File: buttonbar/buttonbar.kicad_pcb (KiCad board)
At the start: 2 copper layers, 65.9 x 54.7 mm, 44 parts, among them J1 Conn_01x08_Male, J2 Conn_01x06_Male, SW1 SW_Push, SW2 SW_Push, SW3 SW_Push, SW4 SW_Push, SW5 SW_Push, SW6 SW_Push, U1 74HC14D

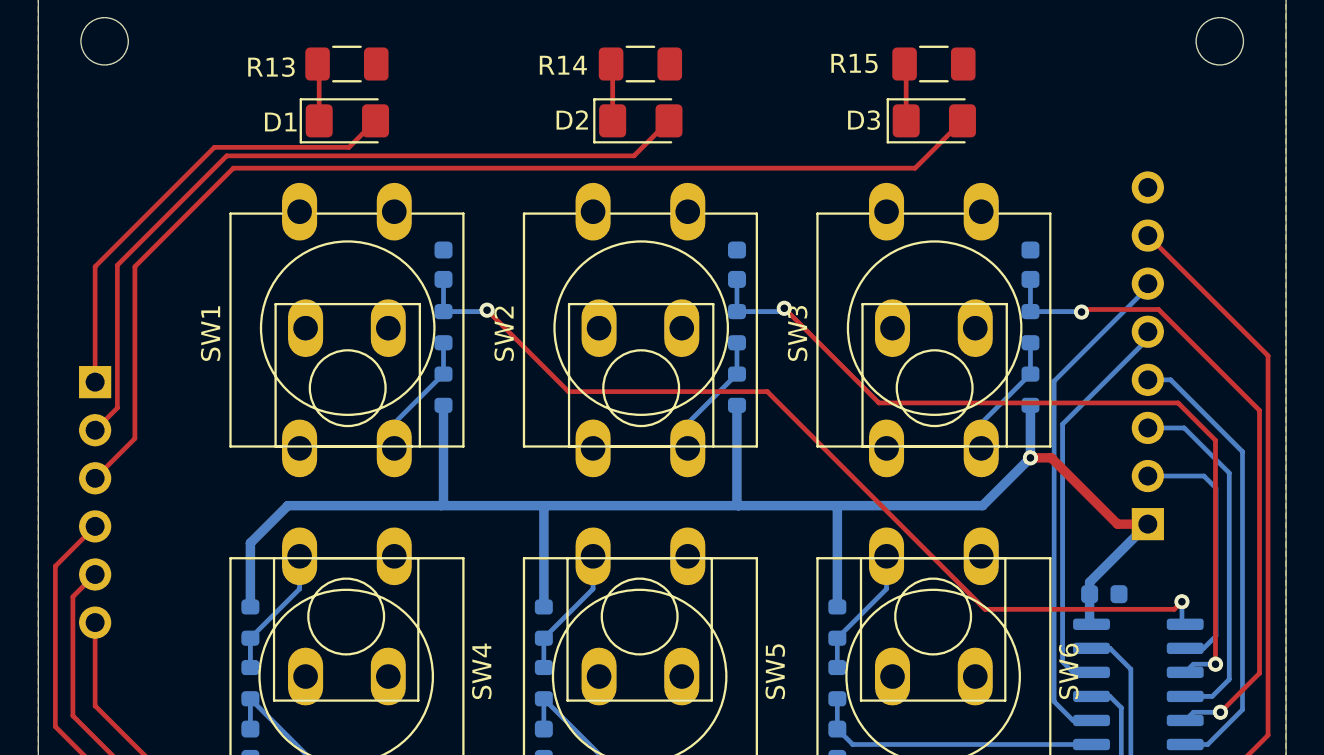
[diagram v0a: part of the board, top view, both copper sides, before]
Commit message: Rev 1.1: added labels (no functional change)
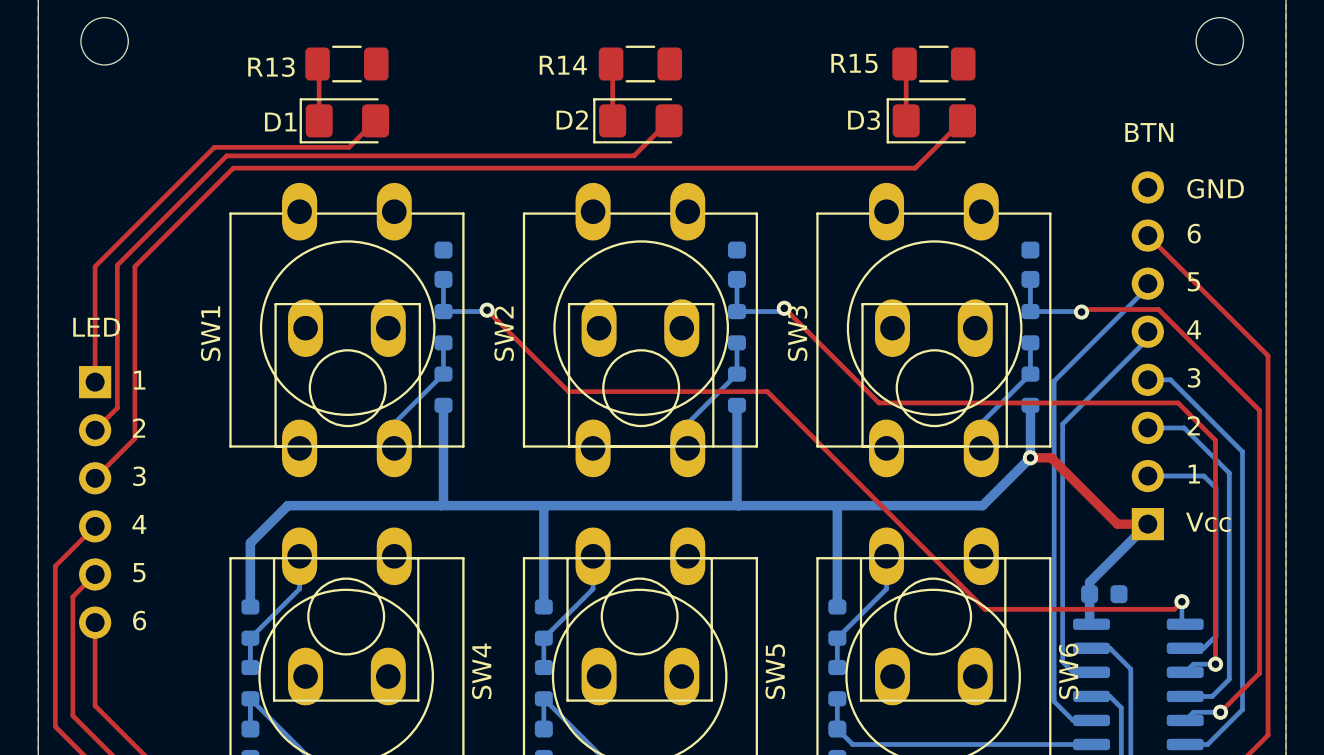
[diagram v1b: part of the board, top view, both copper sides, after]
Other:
- board text added: "2"
- board text added: "3"
- board text added: "4"
- board text added: "5"
- board text added: "6"
- board text added: "BTN"
- board text added: "GND"
- board text added: "LED"
- board text added: "Vcc"
- board text added: "https://github.com/bablokb/pcb-buttonbar Rev 1.1"
- board text removed: "https://github.com/bablokb/pcb-buttonbar Rev 1.0"

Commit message: migrated to Kicad 6
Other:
- net class Default removed
- net class Vcc removed

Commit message: Rev 2.1
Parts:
- added J3: Conn_01x04_Male, Connector_PinHeader_2.54mm:PinHeader_1x04_P2.54mm_Vertical, B.Cu at (149.7, 113.8)
- J1: value Conn_01x08_Male -> Conn_01x04_Male; footprint Connector_PinHeader_2.54mm:PinHeader_1x08_P2.54mm_Vertical -> Connector_PinHeader_2.54mm:PinHeader_1x04_P2.54mm_Vertical
- R13, R14, R15, R16, R17, R18: value 680 1206 -> 680 0603; footprint Resistor_SMD:R_1206_3216Metric_Pad1.30x1.75mm_HandSolder -> Resistor_SMD:R_0603_1608Metric; moved to B.Cu
- SW1, SW2, SW3, SW4, SW5, SW6: footprint user:SW_PUSH-6.12mm -> user:SW_PUSH_5.08mm
- moved H4 80.0 mm to (94.8, 117.0)
- moved J1 69.0 mm to (111.4, 113.8), turned to -90 degrees
- moved H3 67.8 mm to (173.8, 117.0)
- moved H2 61.1 mm to (173.8, 88.0)
- moved C3 57.8 mm to (130.4, 109.4), turned to 0 degrees
- moved R6 57.1 mm to (127.1, 109.4), turned to 180 degrees
- moved R5 56.6 mm to (123.9, 109.4), turned to 0 degrees
- moved C2 55.9 mm to (118.5, 109.4), turned to 0 degrees
- moved R4 54.9 mm to (115.2, 109.4), turned to 180 degrees
- moved C1 54.8 mm to (105.6, 109.6), turned to 0 degrees
- moved R3 54.3 mm to (111.9, 109.4), turned to 0 degrees
- moved R2 53.6 mm to (102.3, 109.6), turned to 180 degrees
- moved R15 53.0 mm to (128.1, 94.9)
- moved R1 52.9 mm to (98.9, 109.6), turned to 0 degrees
- moved R14 51.5 mm to (115.5, 94.9)
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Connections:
- C6 pad 1: Net-(C6-Pad1) -> Net-(U1-Pad13)
- J1 pad 1: /Vcc -> GND
- R12 pad 1: Net-(C6-Pad1) -> Net-(U1-Pad13)
- U1 pad 12: /BTN_4 -> /BTN_6
- U1 pad 13: Net-(C4-Pad1) -> Net-(U1-Pad13)
- U1 pad 8: /BTN_6 -> /BTN_4
- U1 pad 9: Net-(C6-Pad1) -> Net-(C4-Pad1)
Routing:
- net Net-(U1-Pad13): track 0.00 -> 53.8 mm
- net Net-(D3-Pad2): track 58.9 -> 5.74 mm
- net Net-(C4-Pad1): track 60.9 -> 10.8 mm
- net Net-(D2-Pad2): track 41.5 -> 15.4 mm
- net Net-(C3-Pad1): track 34.9 -> 8.96 mm, vias 2 -> 0
- net Net-(D6-Pad2): track 51.2 -> 28.8 mm
- net Net-(D5-Pad2): track 40.2 -> 18.6 mm
- net Net-(D4-Pad2): track 28.9 -> 8.30 mm
- net /BTN_6: track 42.0 -> 22.9 mm, vias 1 -> 0
- net Net-(C2-Pad1): track 43.5 -> 24.7 mm, vias 2 -> 0
- net Net-(C1-Pad1): track 48.7 -> 32.7 mm, vias 2 -> 0
- net Net-(C6-Pad1): track 15.4 -> 0.00 mm
- net /BTN_3: track 24.0 -> 15.2 mm
- net /BTN_1: track 13.6 -> 19.6 mm
- net /Vcc: track 84.7 -> 90.6 mm, vias 1 -> 7
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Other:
- board size 65.9 x 54.7 mm -> 84 x 34 mm
- board text added: "D1"
- board text added: "D2"
- board text added: "D3"
- board text added: "D4"
- board text added: "D5"
- board text added: "D6"
- board text added: "https://github.com/bablokb/pcb-buttonbar Rev 2.1"
- board text removed: "BTN"
- board text removed: "LED"
- board text removed: "https://github.com/bablokb/pcb-buttonbar Rev 1.1"

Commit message: Rev 2.2 (in production)
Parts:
- added H5: MountingHole, MountingHole:MountingHole_2.5mm, F.Cu at (161.1, 88.0)
- added H6: MountingHole, MountingHole:MountingHole_2.5mm, F.Cu at (161.1, 117.0)
- moved C2 1.00 mm to (118.5, 108.4)
- moved C3 1.00 mm to (130.4, 108.4)
- moved C5 1.00 mm to (157.0, 108.4)
- moved C6 1.00 mm to (168.6, 108.4)
- moved R1 1.00 mm to (98.9, 108.6)
- moved R11 1.00 mm to (162.1, 108.4)
- moved R12 1.00 mm to (165.3, 108.4)
- moved R3 1.00 mm to (111.9, 108.4)
- moved R4 1.00 mm to (115.2, 108.4)
- moved R5 1.00 mm to (123.9, 108.4)
- moved R7 1.00 mm to (137.3, 108.4)
- moved R8 1.00 mm to (140.5, 108.4)
- moved R9 1.00 mm to (150.5, 108.4)
- moved C1 1.00 mm to (105.6, 108.6)
- moved R2 1.00 mm to (102.3, 108.6)
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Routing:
- net /BTN_3: track 15.2 -> 13.3 mm
- net Net-(C2-Pad1): track 24.7 -> 26.4 mm
- net Net-(C6-Pad1): track 53.8 -> 52.2 mm
- net Net-(C5-Pad1): track 36.9 -> 35.5 mm
- net Net-(R11-Pad2): track 11.4 -> 10.2 mm
- net Net-(R3-Pad2): track 11.3 -> 10.1 mm
- net Net-(R5-Pad2): track 11.3 -> 10.2 mm
- net Net-(R10-Pad2): track 11.2 -> 10.2 mm
- net Net-(R7-Pad2): track 11.0 -> 9.95 mm
- net Net-(R1-Pad2): track 11.5 -> 10.5 mm
- net /BTN_6: track 22.9 -> 22.0 mm
- net /BTN_5: track 21.0 -> 20.2 mm
- net Net-(C3-Pad1): track 8.96 -> 9.79 mm
- net /BTN_1: track 19.6 -> 20.2 mm
- net /Vcc: track 90.6 -> 90.1 mm
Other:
- board text added: "https://github.com/bablokb/pcb-buttonbar Rev 2.2"
- board text removed: "https://github.com/bablokb/pcb-buttonbar Rev 2.1"
